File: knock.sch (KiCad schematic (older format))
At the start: 17 parts, among them Y1 lfxtal071673

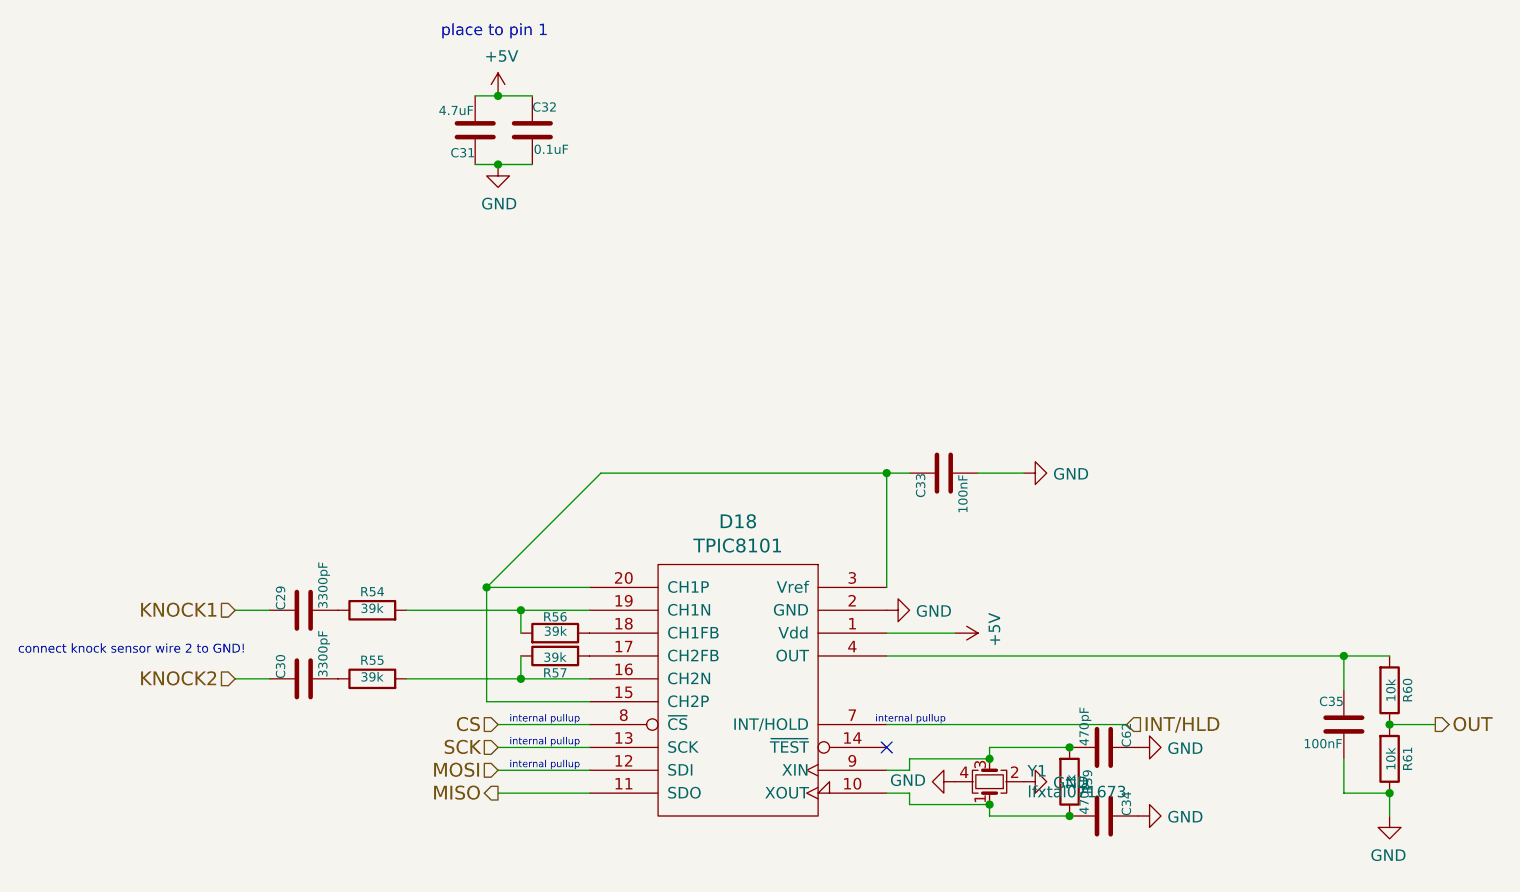
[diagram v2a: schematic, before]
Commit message: added missing component values working on BOM
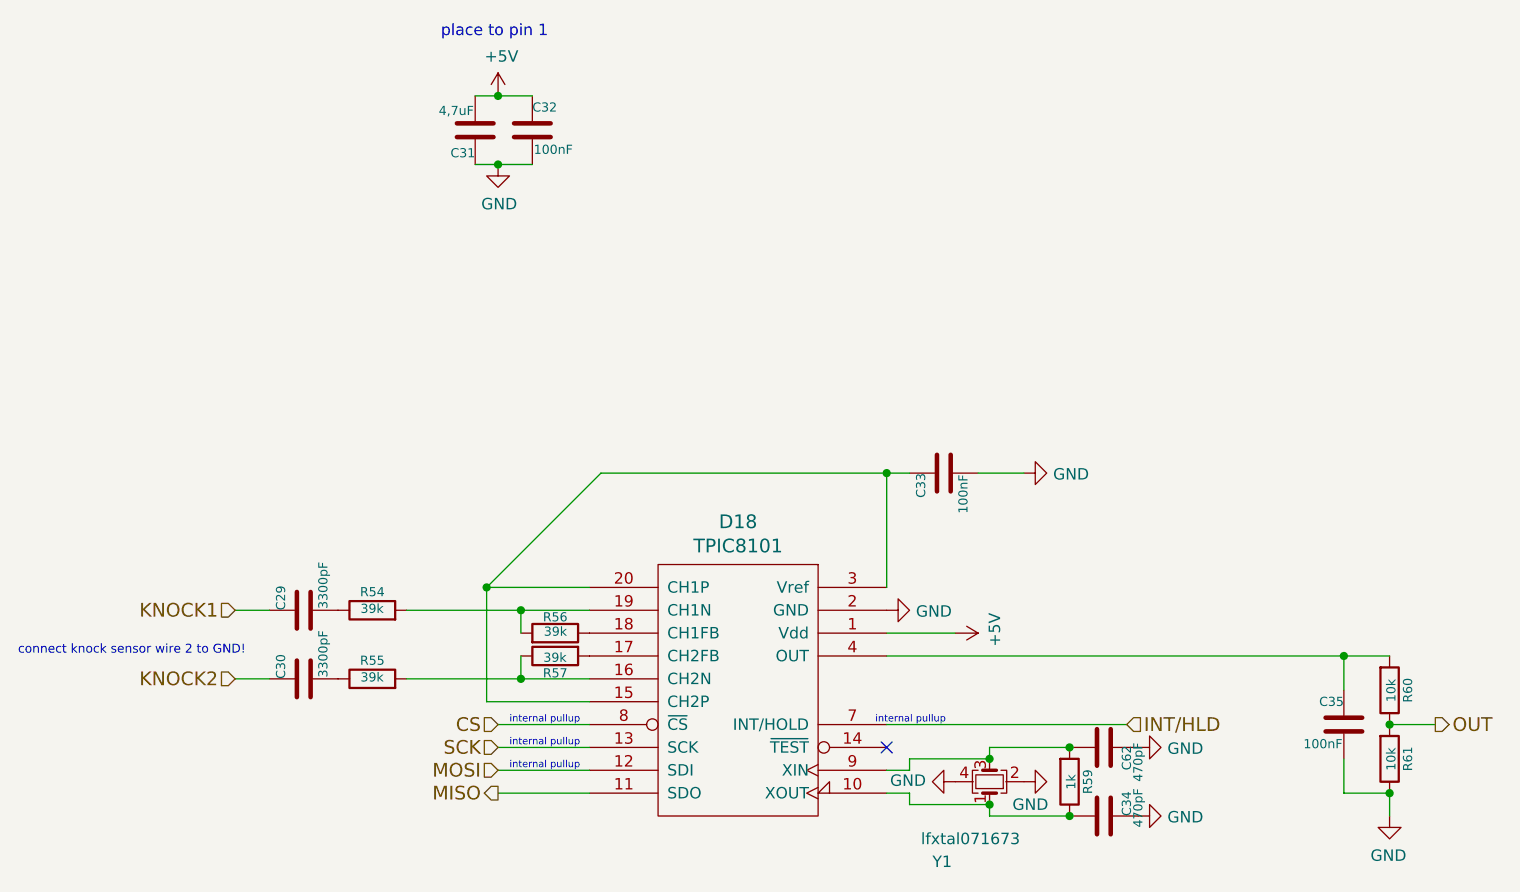
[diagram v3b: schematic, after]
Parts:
- C29, C30: Mouser (none) -> 80-C0805C332K5RAUTO
- C31: value 4.7uF -> 4,7uF; Mouser (none) -> 755-TCSOPL1A226M8R
- C32: value 0.1uF -> 100nF; Mouser (none) -> 80-C0805C104Z3V
- C33, C35: Mouser (none) -> 80-C0805C104Z3V
- C34, C62: Mouser (none) -> 80-C0805C471J5GAUTO
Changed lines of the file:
@@
 P 4900 1600
 F 0 "C32" H 4900 1700 40  0000 L CNN
-F 1 "0.1uF" H 4906 1515 40  0000 L CNN
+F 1 "100nF" H 4906 1515 40  0000 L CNN
 F 2 "Capacitor_SMD:C_0805_2012Metric" H 4938 1450 30  0001 C CNN
 F 3 "~" H 4900 1600 60  0000 C CNN
 F 4 "avx,08055C104KAT2A" H 4900 1600 60  0001 C CNN "MFG,MFG#"
 F 5 "DIGI,478-1395-1-ND" H 4900 1600 60  0001 C CNN "VEND1,VEND1#"
+F 6 "80-C0805C104Z3V " H 4900 1600 50  0001 C CNN "Mouser"
 	1    4900 1600
 	1    0    0    -1
@@
 P 7400 4600
 F 0 "C34" H 7400 4700 40  0000 L CNN
-F 1 "470pF" H 7406 4515 40  0000 L CNN
+F 1 "470pF" H 7350 4750 40  0000 L CNN
 F 2 "Capacitor_SMD:C_0805_2012Metric" V 3080 2000 60  0001 C CNN
 F 3 "" H 7400 4600 60  0001 C CNN
 F 4 "johnson,251R15S240JV4E" V 3080 2000 60  0001 C CNN "MFG,MFG#"
 F 5 "DIGI,712-1383-1-ND" V 3080 2000 60  0001 C CNN "VEND1,VEND1#"
+F 6 "80-C0805C471J5GAUTO" H 7400 4600 50  0001 C CNN "Mouser"
 	1    7400 4600
 	0    1    -1   0
@@
 F 4 "Murata,GRM21B5C1H223JA01L" H 6700 3100 60  0001 C CNN "MFG,MFG#"
 F 5 "DIGI,490-1644-1-ND" H 6700 3100 60  0001 C CNN "VEND1,VEND1#"
+F 6 "80-C0805C104Z3V " H 6700 3100 50  0001 C CNN "Mouser"
 	1    6700 3100
 	0    -1   1    0
@@
 P 4650 1600
 F 0 "C31" H 4650 1700 40  0000 L CNN
-F 1 "4.7uF" H 4656 1515 40  0000 L CNN
+F 1 "4,7uF" H 4656 1515 40  0000 L CNN
 F 2 "Capacitor_SMD:C_0805_2012Metric" V 330 -1600 60  0001 C CNN
 F 3 "" H 4650 1600 60  0001 C CNN
 F 4 "TDK,CGA4J3X5R1H475K125AB" V 330 -1600 60  0001 C CNN "MFG,MFG#"
 F 5 "DIGI,445-7882-6-ND" V 330 -1600 60  0001 C CNN "VEND1,VEND1#"
+F 6 "755-TCSOPL1A226M8R " H 4650 1600 50  0001 C CNN "Mouser"
 	1    4650 1600
 	-1   0    0    1
@@
 F 4 "Murata,GRM2165C1H332JA01D" H 3900 3700 60  0001 C CNN "MFG,MFG#"
 F 5 "DIGI,490-1632-1-ND" H 3900 3700 60  0001 C CNN "VEND1,VEND1#"
+F 6 "80-C0805C332K5RAUTO " H 3900 3700 50  0001 C CNN "Mouser"
 	1    3900 3700
 	0    -1   -1   0
@@
 F 4 "Murata,GRM2165C1H332JA01D" H 3900 4000 60  0001 C CNN "MFG,MFG#"
 F 5 "DIGI,490-1632-1-ND" H 3900 4000 60  0001 C CNN "VEND1,VEND1#"
+F 6 "80-C0805C332K5RAUTO " H 3900 4000 50  0001 C CNN "Mouser"
 	1    3900 4000
 	0    -1   -1   0
@@
 F 4 "Murata,GRM21B5C1H223JA01L" H 8450 4200 60  0001 C CNN "MFG,MFG#"
 F 5 "DIGI,490-1644-1-ND" H 8450 4200 60  0001 C CNN "VEND1,VEND1#"
+F 6 "80-C0805C104Z3V " H 8450 4200 50  0001 C CNN "Mouser"
 	1    8450 4200
 	-1   0    0    -1
@@
 U 1 1 5C0AEC88
 P 6900 4450
-F 0 "Y1" V 6946 4284 50  0000 R CNN
-F 1 "lfxtal071673" V 6855 4284 50  0000 R CNN
+F 0 "Y1" V 6550 4700 50  0000 R CNN
+F 1 "lfxtal071673" V 6650 4750 50  0000 R CNN
 F 2 "boctok_footprints:lfxtal071673" H 7000 4800 50  0001 C CNN
 F 3 "~" H 6900 4450 50  0001 C CNN
@@
 P 7050 4450
 F 0 "#PWR071" H 7050 4200 50  0001 C CNN
-F 1 "GND" V 7055 4322 50  0000 R CNN
+F 1 "GND" V 7150 4500 50  0000 R CNN
 F 2 "" H 7050 4450 50  0001 C CNN
 F 3 "" H 7050 4450 50  0001 C CNN
@@
 U 1 1 5C0AFFB5
 P 7400 4300
-F 0 "C62" H 7400 4400 40  0000 L CNN
-F 1 "470pF" H 7406 4215 40  0000 L CNN
+F 0 "C62" H 7300 4400 40  0000 L CNN
+F 1 "470pF" H 7250 4450 40  0000 L CNN
 F 2 "Capacitor_SMD:C_0805_2012Metric" V 3080 1700 60  0001 C CNN
 F 3 "" H 7400 4300 60  0001 C CNN
 F 4 "johnson,251R15S240JV4E" V 3080 1700 60  0001 C CNN "MFG,MFG#"
 F 5 "DIGI,712-1383-1-ND" V 3080 1700 60  0001 C CNN "VEND1,VEND1#"
+F 6 "80-C0805C471J5GAUTO" H 7400 4300 50  0001 C CNN "Mouser"
 	1    7400 4300
 	0    1    -1   0

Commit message: cleaned BOMs
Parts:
- D18: Mouser (none) -> 595-TPIC8101DWR
- R54, R55, R56, R57: Mouser (none) -> 71-CRCW080539K0FKEA
- R59: Mouser (none) -> 71-CRCW08051K00FKEAC
- R60, R61: Mouser (none) -> 279-CRGCQ0805F10K
- Y1: Mouser (none) -> 449-LFXTAL071673CUTT
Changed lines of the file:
@@
 F 5 "DIGI,CR0805-FX-1002ELFCT-ND" V 4055 4550 60  0001 C CNN "VEND1,VEND1#"
 F 6 "," H 7575 4575 60  0001 C CNN "VEND2,VEND2#"
+F 7 "279-CRGCQ0805F10K" H 8650 4050 50  0001 C CNN "Mouser"
 	1    8650 4050
 	1    0    0    1
@@
 F 5 "DIGI,CR0805-FX-1002ELFCT-ND" V 4055 4350 60  0001 C CNN "VEND1,VEND1#"
 F 6 "," H 7575 4375 60  0001 C CNN "VEND2,VEND2#"
+F 7 "279-CRGCQ0805F10K" H 8650 4350 50  0001 C CNN "Mouser"
 	1    8650 4350
 	1    0    0    1
@@
 F 4 "vishay,CRCW0805820RJNEA" V 1030 3450 60  0001 C CNN "MFG,MFG#"
 F 5 "DIGI,541-820ACT-ND" V 1030 3450 60  0001 C CNN "VEND1,VEND1#"
+F 6 "71-CRCW08051K00FKEAC " H 7250 4450 50  0001 C CNN "Mouser"
 	1    7250 4450
 	1    0    0    1
@@
 F 4 "ECG,ERA6AEB393V" V 2030 3150 60  0001 C CNN "MFG,MFG#"
 F 5 "DIGI,P39KDACT-ND" V 2030 3150 60  0001 C CNN "VEND1,VEND1#"
+F 6 "71-CRCW080539K0FKEA " H 4200 3700 50  0001 C CNN "Mouser"
 	1    4200 3700
 	0    -1   -1   0
@@
 F 4 "ECG,ERA6AEB393V" V 2830 3250 60  0001 C CNN "MFG,MFG#"
 F 5 "DIGI,P39KDACT-ND" V 2830 3250 60  0001 C CNN "VEND1,VEND1#"
+F 6 "71-CRCW080539K0FKEA " H 5000 3800 50  0001 C CNN "Mouser"
 	1    5000 3800
 	0    1    -1   0
@@
 F 4 "ECG,ERA6AEB393V" V 2830 3350 60  0001 C CNN "MFG,MFG#"
 F 5 "DIGI,P39KDACT-ND" V 2830 3350 60  0001 C CNN "VEND1,VEND1#"
+F 6 "71-CRCW080539K0FKEA " H 5000 3900 50  0001 C CNN "Mouser"
 	1    5000 3900
 	0    -1   1    0
@@
 F 4 "ECG,ERA6AEB393V" V 2030 3450 60  0001 C CNN "MFG,MFG#"
 F 5 "DIGI,P39KDACT-ND" V 2030 3450 60  0001 C CNN "VEND1,VEND1#"
+F 6 "71-CRCW080539K0FKEA " H 4200 4000 50  0001 C CNN "Mouser"
 	1    4200 4000
 	0    -1   -1   0
@@
 F 2 "boctok_footprints:TPIC8101" H 6100 4800 60  0001 C CNN
 F 3 "" H 5950 4600 60  0000 C CNN
+F 4 "595-TPIC8101DWR" H 5850 4000 50  0001 C CNN "Mouser"
 	1    5850 4000
 	-1   0    0    -1
@@
 F 2 "boctok_footprints:lfxtal071673" H 7000 4800 50  0001 C CNN
 F 3 "~" H 6900 4450 50  0001 C CNN
+F 4 "449-LFXTAL071673CUTT" H 6900 4450 50  0001 C CNN "Mouser"
 	1    6900 4450
 	0    -1   -1   0
